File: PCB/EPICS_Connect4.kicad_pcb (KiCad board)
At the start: 2 copper layers, 50 x 50 mm, 57 parts, among them J1 USB_C_Receptacle_USB2.0_14P, J2 TC2030, J3 Power, J4 EndA, J5 EndB, J6 LEDA, J7 LEDB, J8 Motor, SW1 ESP.RST, SW2 ESP.BOOT, U2 TPS54202DDC, U3 AP2205-5, U4 SN74AHCT1G125DBVR, U5 ESP32-C3-WROOM-02, U6 SN74AHCT1G125DBVR, U7 STM32G474CBTx

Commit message: Update EPICS_Connect4 KiCad project
Co-Authored-By: Claude Sonnet 5 <noreply@anthropic.com>
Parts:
- added C17: 0.1uF, Capacitor_SMD:C_0603_1608Metric, F.Cu at (134.5, 94.5)
- added C18: 0.1uF, Capacitor_SMD:C_0603_1608Metric, F.Cu at (134.5, 98.5)
- added C19: 1uF, Capacitor_SMD:C_0603_1608Metric, F.Cu at (137.8, 80.5)
- added C20: 10uF, Capacitor_SMD:C_0603_1608Metric, F.Cu at (137.8, 79.0)
- added C21: 10uF, Capacitor_SMD:C_0603_1608Metric, F.Cu at (137.8, 77.5)
- added C22: 1uF, Capacitor_SMD:C_0603_1608Metric, F.Cu at (156.9, 117.0)
- added C23: 100uF, Capacitor_SMD:CP_Elec_6.3x5.9, F.Cu at (167.0, 108.0)
- added D3: 4.5mA @ 1.8V, LED_SMD:LED_0805_2012Metric, F.Cu at (157.8, 92.0)
- added D4: SMF5.0A, Diode_SMD:D_SOD-123F, B.Cu at (133.5, 107.6)
- added D5: SMF5.0A, Diode_SMD:D_SOD-123F, B.Cu at (133.5, 119.6)
- added D6: LED_Small, LED_SMD:LED_0805_2012Metric, F.Cu at (134.0, 126.9)
- added F1: 5A, Fuse:Fuse_1206_3216Metric_Pad1.42x1.75mm_HandSolder, F.Cu at (157.5, 126.5)
- added F2: 2A, Fuse:Fuse_0805_2012Metric_Pad1.15x1.40mm_HandSolder, B.Cu at (134.5, 111.5)
- added F3: 2A, Fuse:Fuse_0805_2012Metric_Pad1.15x1.40mm_HandSolder, B.Cu at (134.5, 123.5)
- added R17: 10k, Resistor_SMD:R_0603_1608Metric, F.Cu at (137.9, 85.0)
- added R18: 5.1k, Resistor_SMD:R_0603_1608Metric, F.Cu at (163.5, 88.2)
- added R19: 5.1k, Resistor_SMD:R_0603_1608Metric, F.Cu at (163.5, 93.8)
- added R20: 22, Resistor_SMD:R_0603_1608Metric, F.Cu at (162.0, 83.5)
- added R21: 22, Resistor_SMD:R_0603_1608Metric, F.Cu at (162.0, 82.0)
- added R23: 330, Resistor_SMD:R_0603_1608Metric, F.Cu at (134.8, 130.0)
- added SYM1: Logo_Open_Hardware_Large, Library:S_Silk_Logo, F.Cu at (154.0, 120.8)
- added TP10: INRP.A, TestPoint:TestPoint_Pad_1.5x1.5mm, B.Cu at (141.2, 91.2)
- added TP11: INRP.B, TestPoint:TestPoint_Pad_1.5x1.5mm, B.Cu at (137.2, 91.2)
- added TP2: GND, TestPoint:TestPoint_Pad_1.0x1.0mm, B.Cu at (154.2, 130.8)
- added TP3: +5V, TestPoint:TestPoint_Pad_1.0x1.0mm, B.Cu at (141.5, 116.0)
- added TP4: GND, TestPoint:TestPoint_Pad_1.0x1.0mm, B.Cu at (141.5, 119.0)
- added TP5: +3V3, TestPoint:TestPoint_Pad_1.0x1.0mm, B.Cu at (147.5, 113.0)
- added TP6: GND, TestPoint:TestPoint_Pad_1.0x1.0mm, B.Cu at (147.5, 116.0)
- added TP7: ST.BOOT, TestPoint:TestPoint_Pad_1.0x1.0mm, B.Cu at (148.0, 104.5)
- added TP8: DataA, TestPoint:TestPoint_Pad_1.0x1.0mm, B.Cu at (135.8, 109.0)
- added TP9: DataB, TestPoint:TestPoint_Pad_1.0x1.0mm, B.Cu at (133.5, 116.0)
- added U1: TPS54202DDC, Package_TO_SOT_SMD:SOT-23-6, F.Cu at (146.0, 127.5)
- added U8: TMC2209, Library:STEPSTICK_socket, F.Cu at (164.0, 108.0)
- C11, C7, C9: value 10uF -> 1uF
- C14, C15: value 1uF -> 0.1uF
- C2: value 0.1uF -> 10uF; footprint Capacitor_SMD:C_0603_1608Metric -> Capacitor_SMD:C_0805_2012Metric
- C3: value 22uF -> 0.1uF; footprint Capacitor_SMD:C_0805_2012Metric -> Capacitor_SMD:C_0603_1608Metric
- C4: value 22uF -> 56pF; footprint Capacitor_SMD:C_0805_2012Metric -> Capacitor_SMD:C_0603_1608Metric
- C5, C6: value 1uF -> 22uF; footprint Capacitor_SMD:C_0603_1608Metric -> Capacitor_SMD:C_0805_2012Metric
- C8: value 56pF -> 10uF
- D1: value 4.5mA @ 1.8V -> SMAJ12A; footprint LED_SMD:LED_0805_2012Metric -> Diode_SMD:D_SMA
- J1: value USB_C_Receptacle_USB2.0_14P -> Power; footprint Connector_USB:USB_C_Receptacle_GCT_USB4110 -> Connector_Molex:Molex_Micro-Fit_3.0_43650-0200_1x02_P3.00mm_Horizontal; moved to B.Cu
- J2: moved to F.Cu
- J3: value Power -> USB_C_Receptacle_USB2.0_14P; footprint Connector_Molex:Molex_Micro-Fit_3.0_43650-0215_1x02_P3.00mm_Vertical -> Connector_USB:USB_C_Receptacle_GCT_USB4110
- J4, J5: footprint Connector_JST:JST_PH_S2B-PH-K_1x02_P2.00mm_Horizontal -> Connector_JST:JST_PH_B2B-PH-K_1x02_P2.00mm_Vertical; moved to B.Cu
- J6, J7, J8: moved to B.Cu
- R1: value 5.1k -> 510k
- R10, R7: value 10k -> 330
- R11, R22: value 5.1k -> 330
- R12: value 22 -> 330
- R13: value 75 -> 330
- R14: value 75 -> 10k
- R15: value 330 -> 10k
- R2: value 22.1k -> 100k
- R3: value 330k -> 22.1k
- R4: value 100k -> 330
- R5: value 56k -> 330
- R9: value 10k -> 5.1k
- SW1, SW2: footprint Button_Switch_THT:SW_PUSH_6mm_H4.3mm -> Button_Switch_SMD:SW_Push_1P1T_NO_CK_KMR2
- TP1: value ST.BOOT -> +12V; moved to B.Cu
- U2: value TPS54202DDC -> AP2205-5; footprint Package_TO_SOT_SMD:SOT-23-6 -> Package_TO_SOT_SMD:SOT-23-5
- U3: value AP2205-5 -> STM32G474CBTx; footprint Package_TO_SOT_SMD:SOT-23-5 -> Package_QFP:LQFP-48_7x7mm_P0.5mm
- U5: value ESP32-C3-WROOM-02 -> SN74AHCT1G125DBVR; footprint RF_Module:ESP32-C3-WROOM-02 -> Package_TO_SOT_SMD:SOT-23-5
- U6: value SN74AHCT1G125DBVR -> ESP32-C3-WROOM-02; footprint Package_TO_SOT_SMD:SOT-23-5 -> RF_Module:ESP32-C3-WROOM-02
- U7: value STM32G474CBTx -> USBLC6-2SC6; footprint Package_QFP:LQFP-48_7x7mm_P0.5mm -> Package_TO_SOT_SMD:SOT-23-6_Handsoldering
- moved R9 83.0 mm to (166.1, 99.5), turned to 180 degrees
- moved C1 72.1 mm to (157.5, 130.8), turned to -90 degrees
- moved C9 70.8 mm to (151.8, 102.8)
- moved R16 69.8 mm to (162.0, 79.0), turned to 180 degrees
- moved R8 62.8 mm to (148.5, 109.5)
- moved L1 62.1 mm to (146.0, 121.0), turned to 90 degrees
- moved C5 61.3 mm to (144.2, 115.5)
- moved C3 61.3 mm to (148.8, 126.0), turned to 90 degrees
- moved R1 60.7 mm to (143.5, 129.7), turned to -90 degrees
- moved U3 60.4 mm to (145.0, 100.0), turned to 180 degrees
- moved R10 59.7 mm to (145.8, 93.2), turned to -90 degrees
- moved C11 58.5 mm to (138.2, 102.8), turned to 180 degrees
- moved C4 57.9 mm to (148.0, 115.5), turned to 180 degrees
- moved C14 57.7 mm to (151.8, 99.8)
- moved R13 57.4 mm to (155.2, 92.8), turned to 90 degrees
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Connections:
- C1 pad 1: GND -> +12V
- C1 pad 2: /Power Regulators/VIN -> GND
- C14 pad 1: +3V3 -> /STM32 Controller/NRST
- C15 pad 1: +3V3 -> /STM32 Controller/INRP.A*
- C16 pad 1: /STM32 Controller/NRST -> /STM32 Controller/INRP.B*
- C2 pad 1: Net-(U2-BOOT) -> GND
- C2 pad 2: Net-(U2-SW) -> +12V
- C3 pad 1: GND -> Net-(U1-BOOT)
- C3 pad 2: /Power Regulators/+3V3 -> Net-(U1-SW)
- C4 pad 1: GND -> Net-(U1-FB)
- C4 pad 2: /Power Regulators/+3V3 -> +3V3
- C5 pad 1: /ESP32 Weblink/EN -> GND
- C5 pad 2: GND -> +3V3
- C6 pad 2: /Power Regulators/VIN -> +3V3
- C7 pad 2: /Power Regulators/+5V -> +12V
- C8 pad 1: Net-(U2-FB) -> GND
- C8 pad 2: /Power Regulators/+3V3 -> +5V
- D1 pad 1: /ESP32 Weblink/LED -> GND
- D1 pad 2: Net-(D1-A) -> +12V
- D2 pad 1: /STM32 Controller/U_LED -> Net-(D2-K)
- D2 pad 2: Net-(D2-A) -> +3V3
- J4 pad 1: unconnected-(J4-Pin_1-Pad1) -> /STM32 Controller/END.A
- J4 pad 2: unconnected-(J4-Pin_2-Pad2) -> GND
- J5 pad 1: unconnected-(J5-Pin_1-Pad1) -> /STM32 Controller/END.B
- J5 pad 2: unconnected-(J5-Pin_2-Pad2) -> GND
- J6 pad 1: unconnected-(J6-Pin_1-Pad1) -> Net-(J6-Pin_1)
- J6 pad 2: unconnected-(J6-Pin_2-Pad2) -> /STM32 Controller/ledDataA
- J6 pad 3: unconnected-(J6-Pin_3-Pad3) -> GND
- J7 pad 1: unconnected-(J7-Pin_1-Pad1) -> Net-(J7-Pin_1)
- J7 pad 2: unconnected-(J7-Pin_2-Pad2) -> /STM32 Controller/ledDataB
- J7 pad 3: unconnected-(J7-Pin_3-Pad3) -> GND
- J8 pad 1: unconnected-(J8-Pin_1-Pad1) -> /Motor Acuator/M10
- J8 pad 2: unconnected-(J8-Pin_2-Pad2) -> /Motor Acuator/M11
- J8 pad 3: unconnected-(J8-Pin_3-Pad3) -> /Motor Acuator/M12
- J8 pad 4: unconnected-(J8-Pin_4-Pad4) -> /Motor Acuator/M13
- L1 pad 1: Net-(U2-SW) -> Net-(U1-SW)
- L1 pad 2: /Power Regulators/+3V3 -> +3V3
- R1 pad 1: Net-(J1-CC1) -> +12V
- R1 pad 2: GND -> Net-(U1-EN)
- R10 pad 1: +3V3 -> Net-(D2-K)
- R10 pad 2: /ESP32 Weblink/IO8 -> /STM32 Controller/U_LED
- R11 pad 1: Net-(J1-CC2) -> Net-(U4-Y)
- R11 pad 2: GND -> /STM32 Controller/ledDataA
- R12 pad 1: Net-(J1-D--PadA7) -> Net-(U5-Y)
- R12 pad 2: /ESP32 Weblink/D- -> /STM32 Controller/ledDataB
- R13 pad 1: Net-(U4-Y) -> +3V3
- R13 pad 2: /STM32 Controller/ledDataA -> Net-(D3-A)
- R14 pad 1: Net-(U6-Y) -> +3V3
- R14 pad 2: /STM32 Controller/ledDataB -> /ESP32 Weblink/EN
- R15 pad 2: Net-(D2-A) -> /ESP32 Weblink/IO9
- R16 pad 1: /STM32 Controller/BOOT -> +3V3
- R16 pad 2: GND -> /ESP32 Weblink/IO2
- R2 pad 1: Net-(U2-FB) -> +3V3
- R2 pad 2: GND -> Net-(U1-FB)
- R22 pad 1: Net-(J1-D+-PadA6) -> +12V
- R22 pad 2: /ESP32 Weblink/D+ -> Net-(D6-A)
- R3 pad 1: /Power Regulators/VIN -> Net-(U1-FB)
- R3 pad 2: /Power Regulators/EN -> GND
- R4 pad 1: /Power Regulators/+3V3 -> /STM32 Controller/INRP.A
- R4 pad 2: Net-(U2-FB) -> /STM32 Controller/INRP.A*
- R5 pad 1: /Power Regulators/EN -> /STM32 Controller/INRP.B
- R5 pad 2: GND -> /STM32 Controller/INRP.B*
- R6 pad 1: +3V3 -> /STM32 Controller/END.A
- R6 pad 2: Net-(D1-A) -> /STM32 Controller/END.A*
- R7 pad 1: +3V3 -> /STM32 Controller/END.B
- R7 pad 2: /ESP32 Weblink/IO2 -> /STM32 Controller/END.B*
- R8 pad 1: +3V3 -> /STM32 Controller/BOOT
- R8 pad 2: /ESP32 Weblink/IO9 -> GND
- R9 pad 2: /ESP32 Weblink/EN -> /Motor Acuator/TMC.PDN
- TP1 pad 1: /STM32 Controller/BOOT -> +12V
- U2 pad 1: GND -> +12V
- U2 pad 2: Net-(U2-SW) -> GND
- U2 pad 3: /Power Regulators/VIN -> +12V
- U2 pad 4: Net-(U2-FB) -> unconnected-(U2-NC-Pad4)
- U2 pad 5: /Power Regulators/EN -> +5V
- U3 pad 1: /Power Regulators/VIN -> +3V3
- U3 pad 2: GND -> unconnected-(U3-PC13-Pad2)
- U3 pad 3: /Power Regulators/VIN -> unconnected-(U3-PC14-Pad3)
- U3 pad 5: /Power Regulators/+5V -> unconnected-(U3-PF0-Pad5)
- U5 pad 1: +3V3 -> GND
- U5 pad 2: /ESP32 Weblink/EN -> /STM32 Controller/LED.B
- U5 pad 3: unconnected-(U5-IO4-Pad3) -> GND
- U5 pad 4: /ESP32 Weblink/BOOT -> Net-(U5-Y)
- U5 pad 5: /ESP32 Weblink/NRST -> +5V
- U6 pad 1: GND -> +3V3
- U6 pad 2: /STM32 Controller/LED.B -> /ESP32 Weblink/EN
- U6 pad 3: GND -> unconnected-(U6-IO4-Pad3)
- U6 pad 4: Net-(U6-Y) -> /STM32 Controller/BOOT
- U6 pad 5: +5V -> /STM32 Controller/NRST
- U7 pad 1: +3V3 -> Net-(J3-D--PadA7)
- U7 pad 2: unconnected-(U7-PC13-Pad2) -> GND
- U7 pad 3: unconnected-(U7-PC14-Pad3) -> Net-(J3-D+-PadA6)
- U7 pad 4: unconnected-(U7-PC15-Pad4) -> /ESP32 Weblink/D.+
- U7 pad 5: unconnected-(U7-PF0-Pad5) -> Net-(U7-VBUS)
- U7 pad 6: unconnected-(U7-PF1-Pad6) -> /ESP32 Weblink/D.-
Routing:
- net /STM32 Controller/NRST: track 0.00 -> 53.3 mm, vias 0 -> 5
- net GND: track 0.00 -> 45.6 mm, vias 0 -> 82
- net /STM32 Controller/BOOT: track 0.00 -> 38.7 mm, vias 0 -> 2
- net +3V3: track 0.00 -> 35.4 mm, vias 0 -> 20
- net /ESP32 Weblink/IO21/TXD: track 0.00 -> 35.2 mm, vias 0 -> 2
- net /ESP32 Weblink/IO20/RXD: track 0.00 -> 34.5 mm, vias 0 -> 2
- net /Motor Acuator/TMC.DIAG: track 0.00 -> 30.5 mm, vias 0 -> 3
- net /STM32 Controller/LED.B: track 0.00 -> 29.2 mm
- net Net-(U1-FB): track 0.00 -> 27.4 mm
- net /Motor Acuator/TMC.EN: track 0.00 -> 27.1 mm
- net +5V: track 0.00 -> 25.1 mm, vias 0 -> 2
- net /ESP32 Weblink/EN: track 0.00 -> 23.9 mm
- net Net-(U7-VBUS): track 0.00 -> 21.7 mm, vias 0 -> 2
- net +12V: track 0.00 -> 19.1 mm, vias 0 -> 18
- net /Motor Acuator/TMC.PDN: track 0.00 -> 18.8 mm
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- added copper zone on B.Cu, net +12V
- added copper zone on F.Cu, net +12V
- added copper zone on In2.Cu, net +12V
- added copper zone on F.Cu, net +3V3
- added copper zone on In2.Cu, net +3V3
- added copper zone on B.Cu, net GND
- added copper zone on F.Cu, net GND
- added copper zone on In1.Cu, net GND
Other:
- board size 50 x 50 mm -> 50 x 60 mm
- copper layers 2 -> 4
- board text added: "9/19/26"
- board text added: "EPICS Klondike"

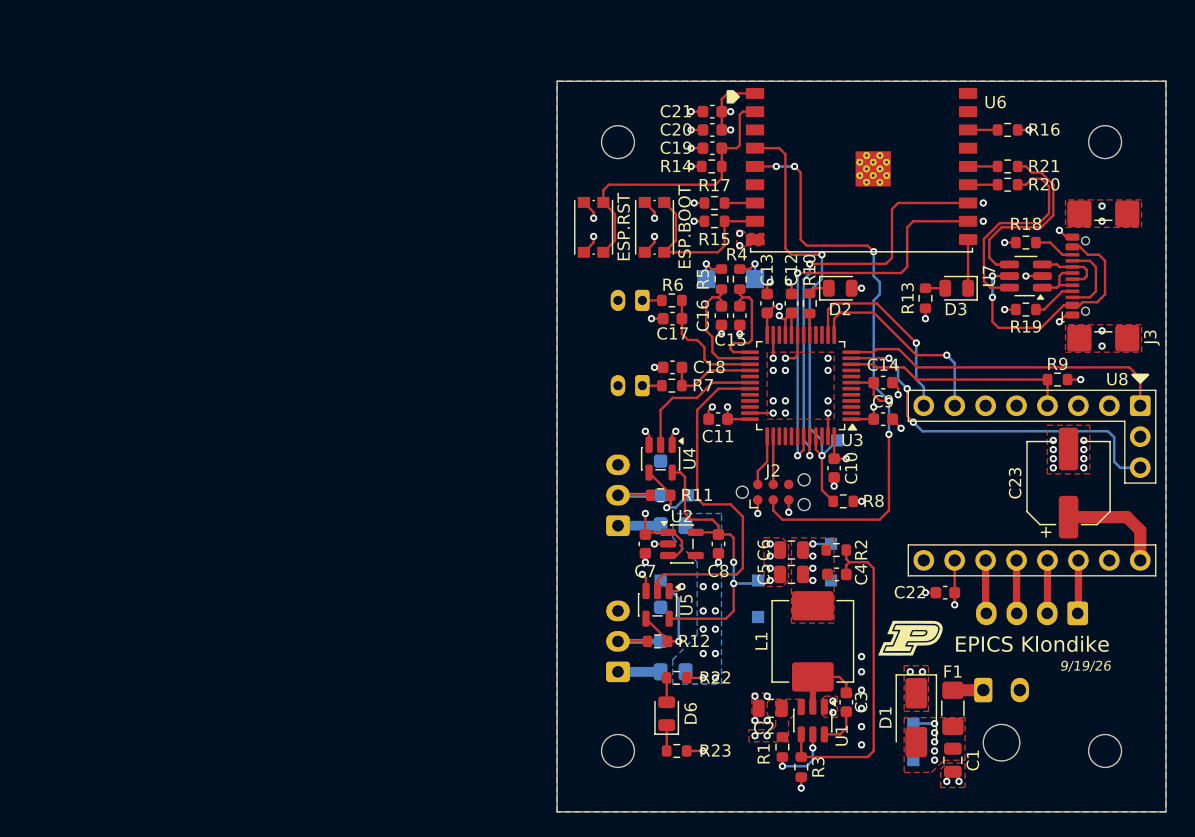
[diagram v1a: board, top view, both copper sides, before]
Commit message: Remove top copper pour
Co-Authored-By: Claude Sonnet 5 <noreply@anthropic.com>
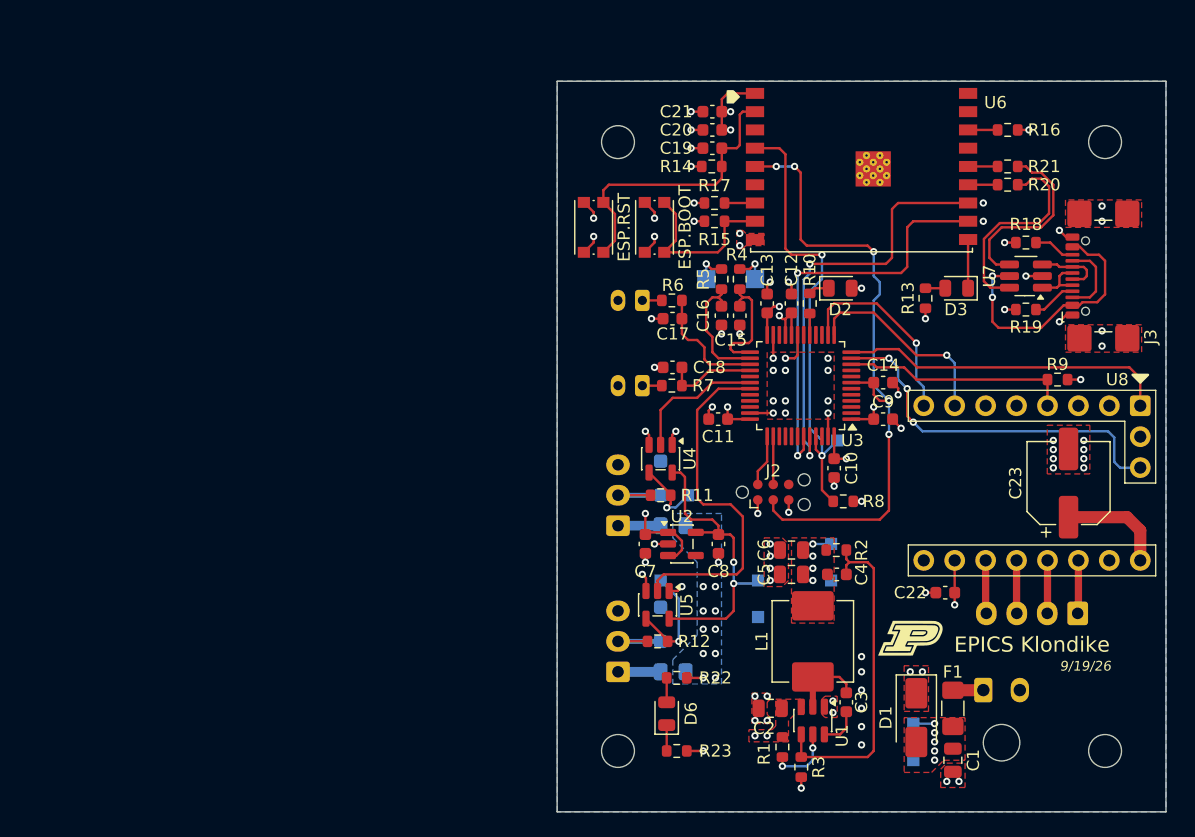
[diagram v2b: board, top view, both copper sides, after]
